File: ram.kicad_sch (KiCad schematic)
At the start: 31 parts, among them SW3 SW_DIP_x08, SW4 SW_Push, U24 74LS245, U25 AS6C6264-55SIN, U26 74LS157, U27 74LS157, U28 74LS04, U29 74LS04, U30 74LS245, U31 74LS00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

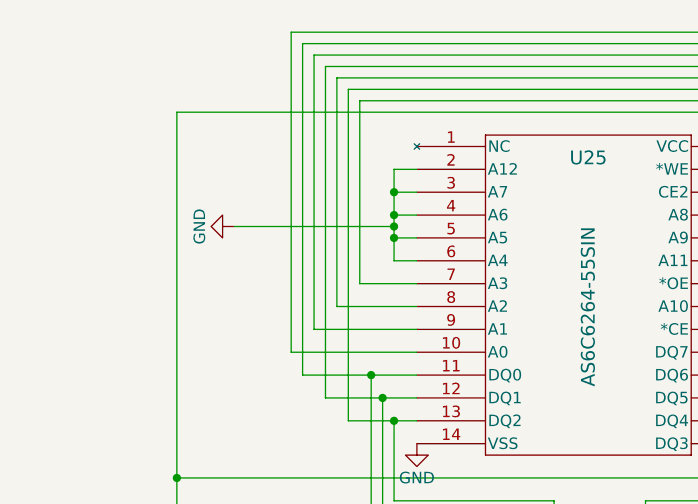
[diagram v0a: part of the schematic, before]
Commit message: Final version
PCB update is missing
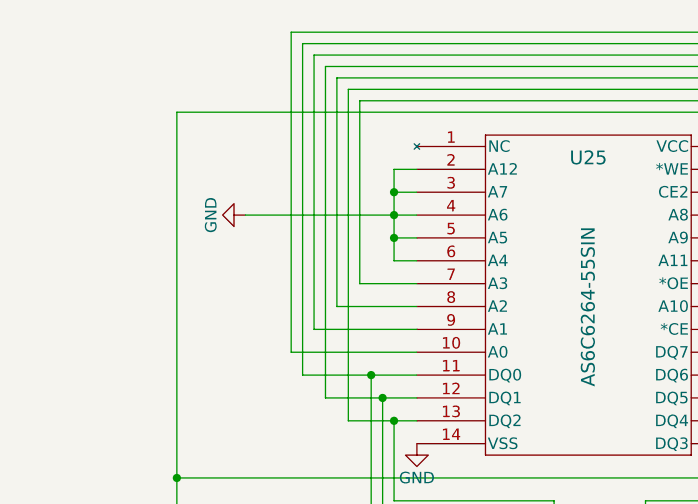
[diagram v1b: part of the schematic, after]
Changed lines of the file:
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@@
   (junction (at 66.04 135.89) (diameter 0) (color 0 0 0 0)
   )
-  (junction (at 54.61 36.83) (diameter 0) (color 0 0 0 0)
-  )
   (junction (at 97.79 38.1) (diameter 0) (color 0 0 0 0)
   )
@@
     (stroke (width 0) (type default))
   )
+  (wire (pts (xy 38.1 35.56) (xy 54.61 35.56))
+    (stroke (width 0) (type default))
+  )
   (wire (pts (xy 138.43 36.83) (xy 123.19 36.83))
     (stroke (width 0) (type default))
@@
     (stroke (width 0) (type default))
   )
-  (wire (pts (xy 54.61 36.83) (xy 54.61 38.1))
+  (wire (pts (xy 54.61 35.56) (xy 54.61 38.1))
     (stroke (width 0) (type default))
   )
@@
     (stroke (width 0) (type default))
   )
-  (wire (pts (xy 36.83 36.83) (xy 54.61 36.83))
-    (stroke (width 0) (type default))
-  )
   (wire (pts (xy 104.14 135.89) (xy 104.14 132.08))
     (stroke (width 0) (type default))
@@
     (stroke (width 0) (type default))
   )
-  (wire (pts (xy 54.61 35.56) (xy 54.61 36.83))
-    (stroke (width 0) (type default))
-  )
   (wire (pts (xy 200.66 99.06) (xy 256.54 99.06))
     (stroke (width 0) (type default))
@@
   (symbol (lib_id "power:VCC") (at 95.25 27.94 0) (unit 1)
     (in_bom yes) (on_board yes) (dnp no)
-    (property "Reference" "#PWR01" (at 95.25 31.75 0)
+    (property "Reference" "#PWR0104" (at 95.25 31.75 0)
       (effects (font (size 1.27 1.27)) hide)
     )
@@
     (pin "1")
     (instances
+      (project "8bit-computer"
+        (path "/6b77b9f1-1099-4db3-bd4e-d48066f72e59/00000000-0000-0000-0000-00005b551e96"
+          (reference "#PWR0104") (unit 1)
+        )
+      )
       (project "ram"
         (path "/c8f4549e-1433-4994-b3c8-85097e8cdb88"
@@
     )
   )
-  (symbol (lib_id "power:GND") (at 36.83 36.83 270) (unit 1)
+  (symbol (lib_id "power:GND") (at 38.1 35.56 270) (unit 1)
     (in_bom yes) (on_board yes) (dnp no)
-    (property "Reference" "#PWR02" (at 30.48 36.83 0)
+    (property "Reference" "#PWR0103" (at 31.75 35.56 0)
       (effects (font (size 1.27 1.27)) hide)
     )
-    (property "Value" "GND" (at 33.02 36.83 0)
+    (property "Value" "GND" (at 34.29 35.56 0)
       (effects (font (size 1.27 1.27)))
     )
-    (property "Footprint" "" (at 36.83 36.83 0)
+    (property "Footprint" "" (at 38.1 35.56 0)
       (effects (font (size 1.27 1.27)) hide)
     )
-    (property "Datasheet" "" (at 36.83 36.83 0)
+    (property "Datasheet" "" (at 38.1 35.56 0)
       (effects (font (size 1.27 1.27)) hide)
     )
     (pin "1")
     (instances
+      (project "8bit-computer"
+        (path "/6b77b9f1-1099-4db3-bd4e-d48066f72e59/00000000-0000-0000-0000-00005b551e96"
+          (reference "#PWR0103") (unit 1)
+        )
+      )
       (project "ram"
         (path "/c8f4549e-1433-4994-b3c8-85097e8cdb88"
@@
   (symbol (lib_id "power:GND") (at 57.15 60.96 0) (unit 1)
     (in_bom yes) (on_board yes) (dnp no)
-    (property "Reference" "#PWR03" (at 57.15 67.31 0)
+    (property "Reference" "#PWR0102" (at 57.15 67.31 0)
       (effects (font (size 1.27 1.27)) hide)
     )
@@
     (pin "1")
     (instances
+      (project "8bit-computer"
+        (path "/6b77b9f1-1099-4db3-bd4e-d48066f72e59/00000000-0000-0000-0000-00005b551e96"
+          (reference "#PWR0102") (unit 1)
+        )
+      )
       (project "ram"
         (path "/c8f4549e-1433-4994-b3c8-85097e8cdb88"

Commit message: Updated version
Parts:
- removed U28, U29: 74LS04, Package_DIP:DIP-14_W7.62mm, symbol 8bit-computer-rescue:74LS04-8bit-computer-rescue
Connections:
- net at U24.2 (A0), U25.11 (DQ0): now also D36.2 (A), U30.2 (A0)
- net at U24.3 (A1), U25.12 (DQ1): now also D37.2 (A), U30.3 (A1)
- net at U24.4 (A2), U25.13 (DQ2): now also D38.2 (A), U30.4 (A2)
- net at D39.2 (A), U30.5 (A3): now also U24.5 (A3), U25.15 (DQ3)
- net at U24.9 (A7), U25.19 (DQ7): now also D43.2 (A), U30.9 (A7)
- net at U24.8 (A6), U25.18 (DQ6): now also D42.2 (A), U30.8 (A6)
- net at U24.7 (A5), U25.17 (DQ5): now also D41.2 (A), U30.7 (A5)
- net at D40.2 (A), U30.6 (A4): now also U24.6 (A4), U25.16 (DQ4)
- no-connect marks 26 -> 18
